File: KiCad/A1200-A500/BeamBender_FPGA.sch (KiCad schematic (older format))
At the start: 15 parts, among them J6 Conn_02x06_Odd_Even, U2 GW1NR-UV9LQ144P, U5 AK5720VT, X3 5.0x3.2mm

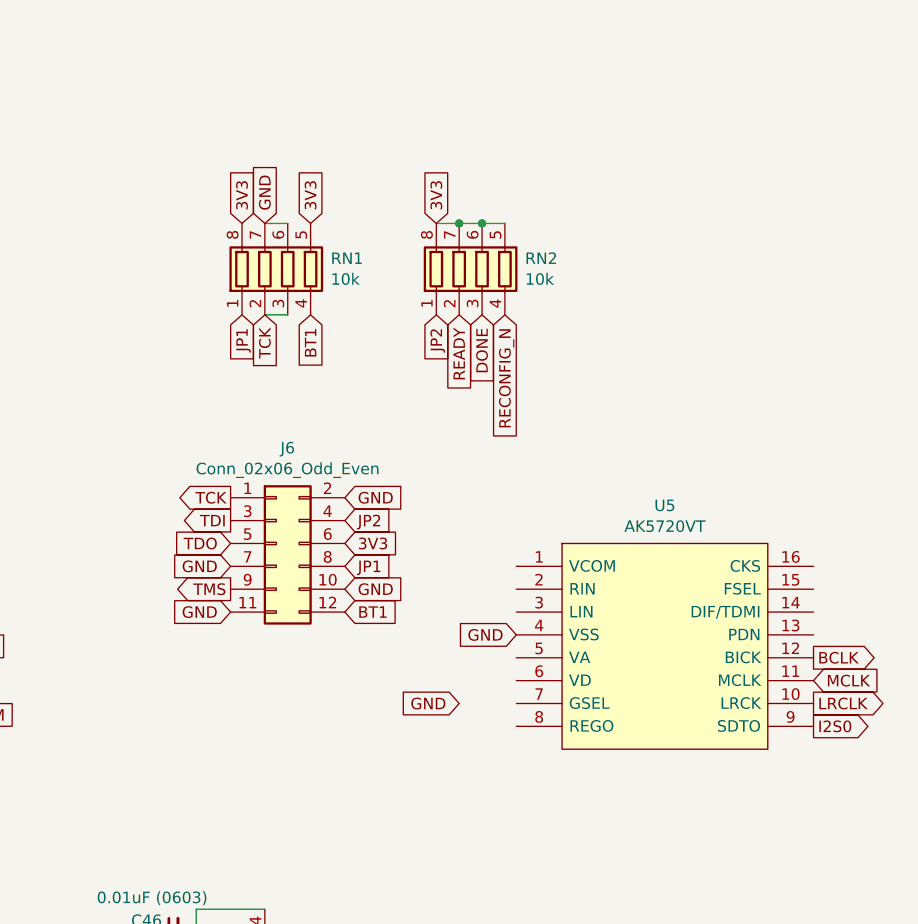
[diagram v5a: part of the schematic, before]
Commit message: Added series resistors to BCLK, LRCLK and I2S0 audio lines.
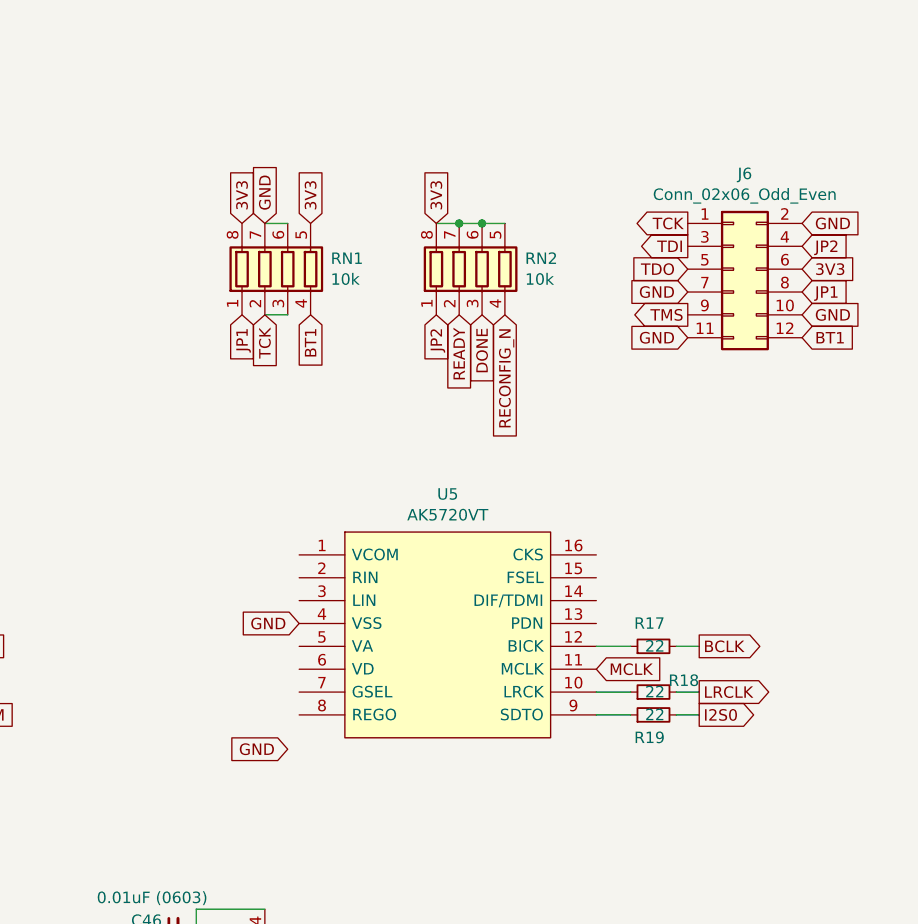
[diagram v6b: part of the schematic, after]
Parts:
- added R17, R18, R19: 22, Resistor_SMD:R_0603_1608Metric_Pad0.98x0.95mm_HandSolder, symbol Device:R_Small
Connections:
- net BCLK: now also R17.2; no longer U5.12 (BICK)
- net I2S0: now also R19.2; no longer U5.9 (SDTO)
- net LRCLK: now also R18.2; no longer U5.10 (LRCK)
- new net: R18.1, U5.10 (LRCK)
- new net: R17.1, U5.12 (BICK)
- new net: R19.1, U5.9 (SDTO)
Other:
- moved on the sheet: J6, U5
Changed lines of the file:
@@
 Text GLabel 8400 2200 3    50   Input ~ 0
 BT1
-Text GLabel 8050 3000 0    50   Output ~ 0
+Text GLabel 10050 1800 0    50   Output ~ 0
 TCK
-Text GLabel 8050 3100 0    50   Output ~ 0
+Text GLabel 10050 1900 0    50   Output ~ 0
 TDI
-Text GLabel 8050 3200 0    50   Input ~ 0
+Text GLabel 10050 2000 0    50   Input ~ 0
 TDO
-Text GLabel 8050 3300 0    50   Input ~ 0
-GND
-Text GLabel 8050 3400 0    50   Output ~ 0
+Text GLabel 10050 2100 0    50   Input ~ 0
+GND
+Text GLabel 10050 2200 0    50   Output ~ 0
 TMS
-Text GLabel 8550 3000 2    50   Input ~ 0
-GND
-Text GLabel 8550 3400 2    50   Input ~ 0
-GND
-Text GLabel 8550 3200 2    50   Input ~ 0
+Text GLabel 10550 1800 2    50   Input ~ 0
+GND
+Text GLabel 10550 2200 2    50   Input ~ 0
+GND
+Text GLabel 10550 2000 2    50   Input ~ 0
 3V3
 Text GLabel 1600 4500 0    50   Input ~ 0
@@
 BT1
 NoConn ~ 1600 3200
-Text GLabel 8550 3300 2    50   Input ~ 0
+Text GLabel 10550 2100 2    50   Input ~ 0
 JP1
-Text GLabel 8550 3100 2    50   Input ~ 0
+Text GLabel 10550 1900 2    50   Input ~ 0
 JP2
 Wire Wire Line
@@
 Text GLabel 8100 1800 1    50   Input ~ 0
 3V3
-Text GLabel 8550 3500 2    50   Input ~ 0
+Text GLabel 10550 2300 2    50   Input ~ 0
 BT1
-Text GLabel 8050 3500 0    50   Input ~ 0
+Text GLabel 10050 2300 0    50   Input ~ 0
 GND
 $Comp
 L Connector_Generic:Conn_02x06_Odd_Even J6
 U 1 1 663407EE
-P 8250 3200
-F 0 "J6" H 8300 3617 50  0000 C CNN
-F 1 "Conn_02x06_Odd_Even" H 8300 3526 50  0000 C CNN
-F 2 "Connector_PinHeader_2.54mm:PinHeader_2x06_P2.54mm_Horizontal" H 8250 3200 50  0001 C CNN
-F 3 "~" H 8250 3200 50  0001 C CNN
-	1    8250 3200
+P 10250 2000
+F 0 "J6" H 10300 2417 50  0000 C CNN
+F 1 "Conn_02x06_Odd_Even" H 10300 2326 50  0000 C CNN
+F 2 "Connector_PinHeader_2.54mm:PinHeader_2x06_P2.54mm_Horizontal" H 10250 2000 50  0001 C CNN
+F 3 "~" H 10250 2000 50  0001 C CNN
+	1    10250 2000
 	1    0    0    -1
 $EndComp
@@
 L BeamBender:AK5720VT U5
 U 1 1 665688C0
-P 9950 3650
-F 0 "U5" H 9950 4265 50  0000 C CNN
-F 1 "AK5720VT" H 9950 4174 50  0000 C CNN
-F 2 "Package_SO:TSSOP-16_4.4x5mm_P0.65mm" H 11100 3750 50  0001 L CNN
-F 3 "" H 11100 3650 50  0001 L CNN
-F 4 "24-bit Audio ADC" H 11100 3550 50  0001 L CNN "Description"
-	1    9950 3650
-	1    0    0    -1
-$EndComp
-Text GLabel 9050 3900 0    50   Input ~ 0
-GND
-Text GLabel 9300 3600 0    50   Input ~ 0
-GND
-Text GLabel 10600 4000 2    50   Output ~ 0
+P 9000 3600
+F 0 "U5" H 9000 4215 50  0000 C CNN
+F 1 "AK5720VT" H 9000 4124 50  0000 C CNN
+F 2 "Package_SO:TSSOP-16_4.4x5mm_P0.65mm" H 10150 3700 50  0001 L CNN
+F 3 "" H 10150 3600 50  0001 L CNN
+F 4 "24-bit Audio ADC" H 10150 3500 50  0001 L CNN "Description"
+	1    9000 3600
+	1    0    0    -1
+$EndComp
+Text GLabel 8300 4100 0    50   Input ~ 0
+GND
+Text GLabel 8350 3550 0    50   Input ~ 0
+GND
+Text GLabel 10100 3950 2    50   Output ~ 0
 I2S0
-Text GLabel 10600 3800 2    50   Input ~ 0
+Text GLabel 9650 3750 2    50   Input ~ 0
 MCLK
-Text GLabel 10600 3900 2    50   Output ~ 0
+Text GLabel 10100 3850 2    50   Output ~ 0
 LRCLK
-Text GLabel 10600 3700 2    50   Output ~ 0
+Text GLabel 10100 3650 2    50   Output ~ 0
 BCLK
 Text GLabel 7900 5100 0    50   Input ~ 0
@@
 Wire Wire Line
 	1350 4600 1600 4600
+$Comp
+L Device:R_Small R17
+U 1 1 666AAB38
+P 9900 3650
+F 0 "R17" V 10000 3600 50  0000 L CNN
+F 1 "22" V 9900 3600 50  0000 L CNN
+F 2 "Resistor_SMD:R_0603_1608Metric_Pad0.98x0.95mm_HandSolder" H 9900 3650 50  0001 C CNN
+F 3 "~" H 9900 3650 50  0001 C CNN
+	1    9900 3650
+	0    -1   -1   0
+$EndComp
+$Comp
+L Device:R_Small R18
+U 1 1 666AD788
+P 9900 3850
+F 0 "R18" V 9950 3650 50  0000 L CNN
+F 1 "22" V 9900 3800 50  0000 L CNN
+F 2 "Resistor_SMD:R_0603_1608Metric_Pad0.98x0.95mm_HandSolder" H 9900 3850 50  0001 C CNN
+F 3 "~" H 9900 3850 50  0001 C CNN
+	1    9900 3850
+	0    -1   -1   0
+$EndComp
+$Comp
+L Device:R_Small R19
+U 1 1 666AF72B
+P 9900 3950
+F 0 "R19" V 9800 3900 50  0000 L CNN
+F 1 "22" V 9900 3900 50  0000 L CNN
+F 2 "Resistor_SMD:R_0603_1608Metric_Pad0.98x0.95mm_HandSolder" H 9900 3950 50  0001 C CNN
+F 3 "~" H 9900 3950 50  0001 C CNN
+	1    9900 3950
+	0    -1   -1   0
+$EndComp
+Wire Wire Line
+	9650 3950 9800 3950
+Wire Wire Line
+	9650 3850 9800 3850
+Wire Wire Line
+	9650 3650 9800 3650
+Wire Wire Line
+	10000 3650 10100 3650
+Wire Wire Line
+	10000 3850 10100 3850
+Wire Wire Line
+	10000 3950 10100 3950
 $EndSCHEMATC

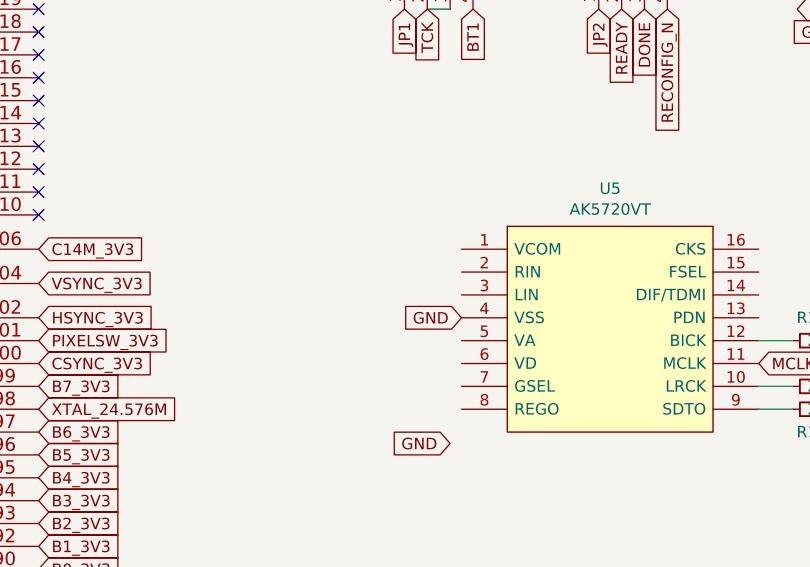
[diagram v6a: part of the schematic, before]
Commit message: assigned the audio Left and Right channels to 3.5mm phono jack (STX-3501-3N) and to ADC-chip (AK5720)
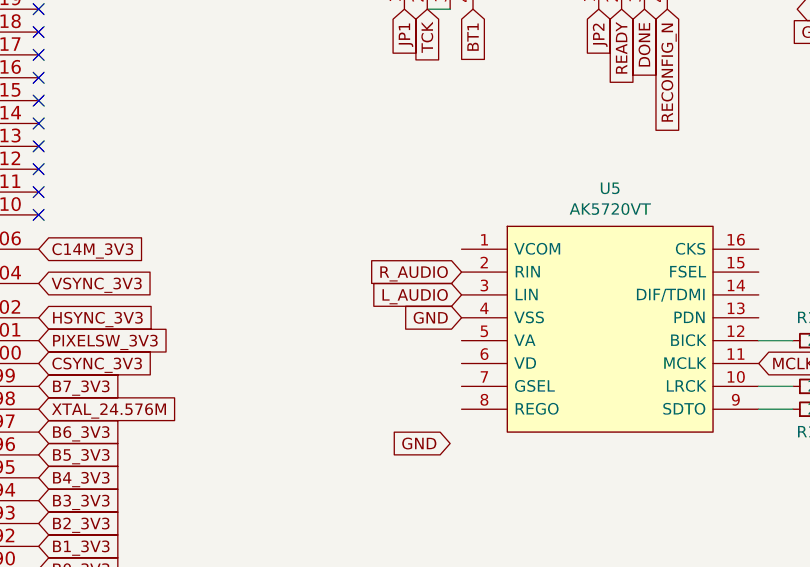
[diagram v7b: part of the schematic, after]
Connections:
- net R_AUDIO: now reaches U5.2 (RIN)
- net L_AUDIO: now reaches U5.3 (LIN)
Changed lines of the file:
@@
 Wire Wire Line
 	10000 3950 10100 3950
+Text GLabel 8350 3450 0    50   Input ~ 0
+L_AUDIO
+Text GLabel 8350 3350 0    50   Input ~ 0
+R_AUDIO
 $EndSCHEMATC

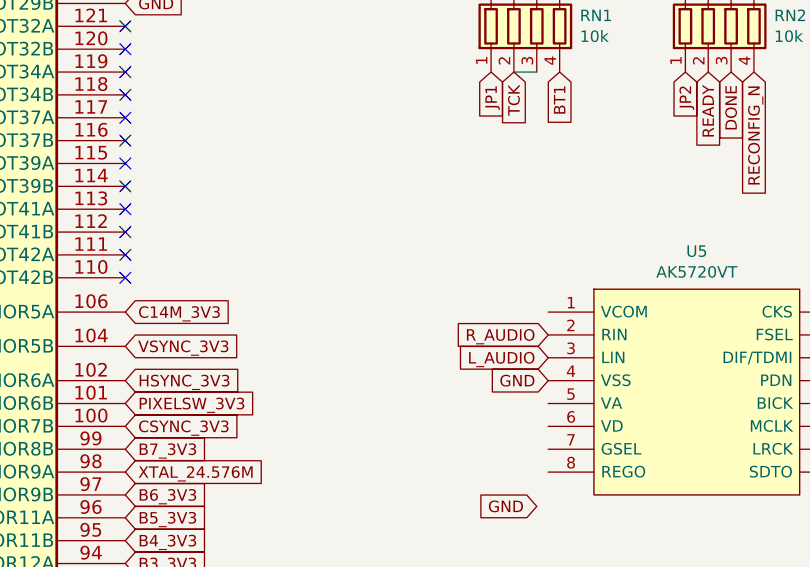
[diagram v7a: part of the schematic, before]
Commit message: Added coupling caps for analogue left and right channel to inputs on ADC-chip (AK5720VT)
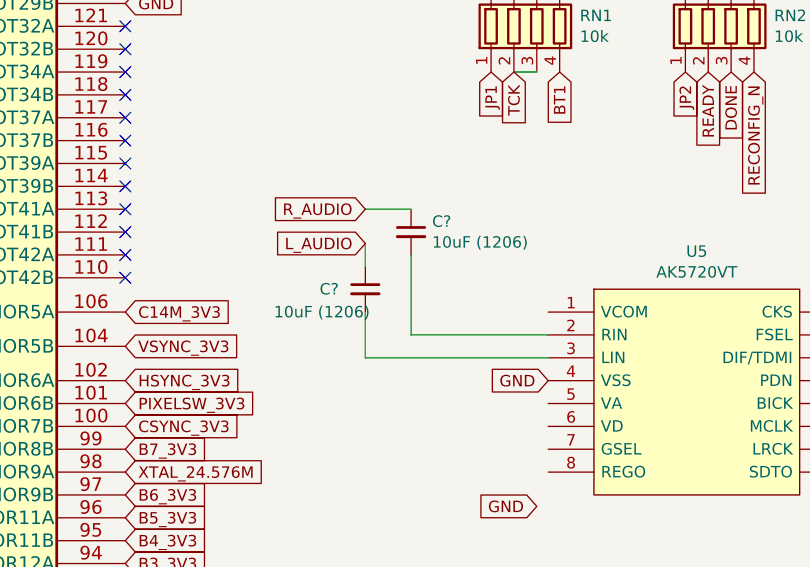
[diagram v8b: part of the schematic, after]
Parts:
- added C? (x2): 10uF (1206), Capacitor_SMD:C_1206_3216Metric_Pad1.33x1.80mm_HandSolder, symbol Device:C_Small
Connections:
- net L_AUDIO: now also C?.1; no longer U5.3 (LIN)
- net R_AUDIO: now also C?.1; no longer U5.2 (RIN)
- new net: C?.2, U5.2 (RIN)
- new net: C?.2, U5.3 (LIN)
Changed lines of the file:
@@
 Wire Wire Line
 	10000 3950 10100 3950
-Text GLabel 8350 3450 0    50   Input ~ 0
+Text GLabel 7550 2950 0    50   Input ~ 0
 L_AUDIO
-Text GLabel 8350 3350 0    50   Input ~ 0
+Text GLabel 7550 2800 0    50   Input ~ 0
 R_AUDIO
+$Comp
+L Device:C_Small C?
+U 1 1 667B6179
+P 7750 2900
+F 0 "C?" H 7842 2946 50  0000 L CNN
+F 1 "10uF (1206)" H 7842 2855 50  0000 L CNN
+F 2 "Capacitor_SMD:C_1206_3216Metric_Pad1.33x1.80mm_HandSolder" H 7750 2900 50  0001 C CNN
+F 3 "~" H 7750 2900 50  0001 C CNN
+	1    7750 2900
+	1    0    0    -1
+$EndComp
+$Comp
+L Device:C_Small C?
+U 1 1 667B7F1E
+P 7550 3150
+F 0 "C?" H 7350 3150 50  0000 L CNN
+F 1 "10uF (1206)" H 7150 3050 50  0000 L CNN
+F 2 "Capacitor_SMD:C_1206_3216Metric_Pad1.33x1.80mm_HandSolder" H 7550 3150 50  0001 C CNN
+F 3 "~" H 7550 3150 50  0001 C CNN
+	1    7550 3150
+	1    0    0    -1
+$EndComp
+Wire Wire Line
+	8350 3450 7550 3450
+Wire Wire Line
+	7550 3450 7550 3250
+Wire Wire Line
+	7550 2800 7750 2800
+Wire Wire Line
+	7750 3000 7750 3350
+Wire Wire Line
+	7750 3350 8350 3350
+Wire Wire Line
+	7550 2950 7550 3050
 $EndSCHEMATC
